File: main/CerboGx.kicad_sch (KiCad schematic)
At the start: 1 part

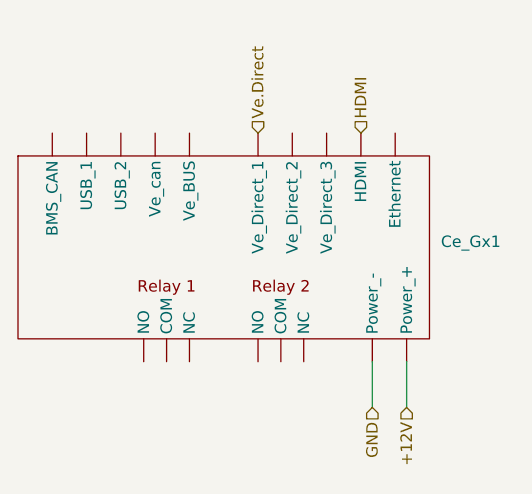
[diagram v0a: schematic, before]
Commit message: added UI, +12/gnd to 4 pin adapter symbol, added NMEA2000 gateway symbol
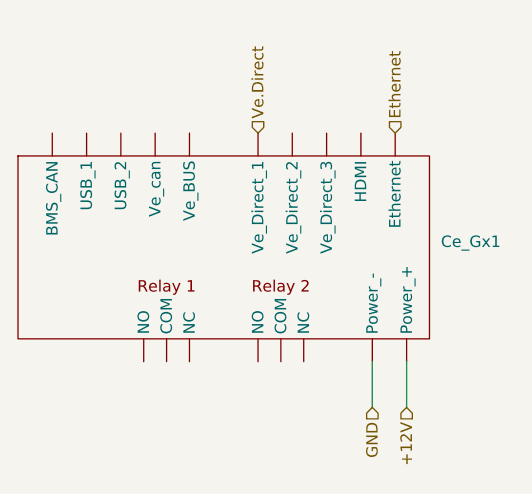
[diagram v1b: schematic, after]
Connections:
- net HDMI is gone; now on net Ve.Direct: Ce_Gx1. (Ve_can)
- new net Ethernet: Ce_Gx1. (Ve_can)
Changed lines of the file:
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@@
 		)
 	)
-	(hierarchical_label "HDMI"
+	(hierarchical_label "Ethernet"
 		(shape input)
-		(at 157.48 78.74 90)
+		(at 161.29 78.74 90)
 		(fields_autoplaced yes)
 		(effects

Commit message: added logos, oranised sheets, final version
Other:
- company: (none) -> Designers: Krzysztof Grajek, Wojtek Kołodziej
- title: (none) -> Cerbo GX schematic
